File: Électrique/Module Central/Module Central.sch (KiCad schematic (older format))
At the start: 31 parts, among them J101 2.1mm X 5.5mm Barrel Connector, J102 Prog, J103 Conn_Coaxial, U101 LM2937xMP, U102 ATmega328P-AU, U103 RMF95, U104 FXMA108, Y101 16MHz

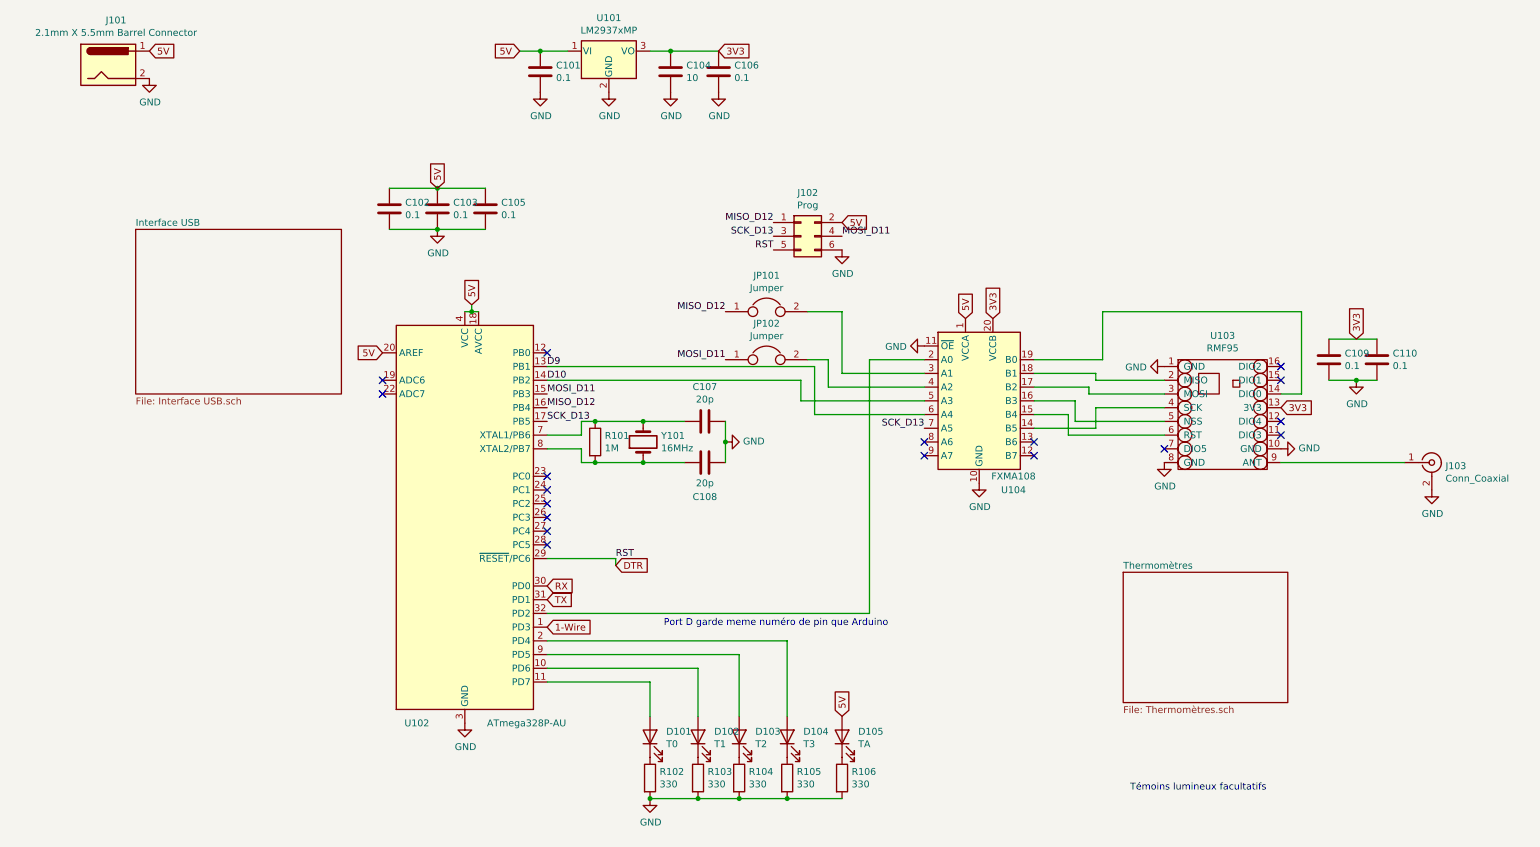
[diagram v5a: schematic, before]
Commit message: Modification PCB
Changement des Level shifters pour des pieces disponibles
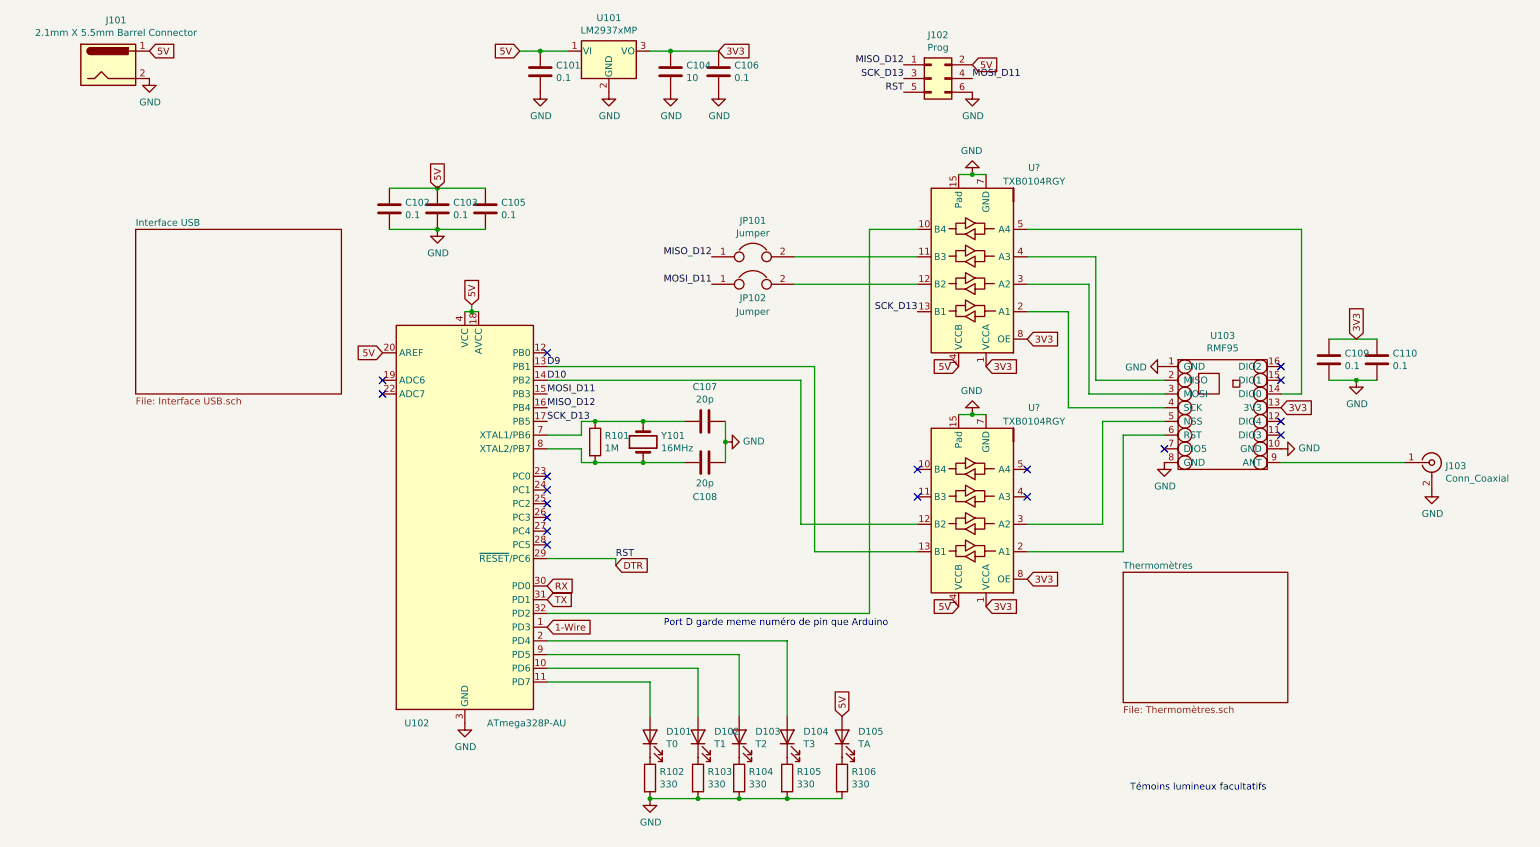
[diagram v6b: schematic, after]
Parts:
- removed U104: FXMA108, Package_DFN_QFN:WQFN-20-1EP_2.5x4.5mm_P0.5mm_EP1x2.9mm, symbol Logic_LevelTranslator:FXMA108
- added U? (x2): TXB0104RGY, Package_DFN_QFN:Texas_S-PVQFN-N14, symbol Logic_LevelTranslator:TXB0104RGY
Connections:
- net 3V3: now also U?.1 (VCCA), U?.1 (VCCA), U?.8 (OE), U?.8 (OE)
- net 5V: now also U?.14 (VCCB), U?.14 (VCCB)
- net D10: now also U?.12 (B2)
- net D9: now also U?.13 (B1)
- net GND: now also U?.15 (Pad), U?.15 (Pad), U?.7 (GND), U?.7 (GND)
- net SCK_D13: now also U?.13 (B1)
- net at U102.32 (PD2): now also U?.10 (B4)
- net at U103.14 (DIO0): now also U?.5 (A4)
- net at U103.2 (MISO): now also U?.4 (A3)
- net at U103.3 (MOSI): now also U?.3 (A2)
- net at U103.4 (SCK): now also U?.2 (A1)
- net at U103.5 (NSS): now also U?.3 (A2)
- net at U103.6 (RST): now also U?.2 (A1)
- net at JP101.2: now also U?.11 (B3)
- net at JP102.2: now also U?.12 (B2)
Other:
- moved on the sheet: J102, JP101, JP102
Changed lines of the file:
@@
 L Connector_Generic:Conn_02x03_Odd_Even J102
 U 1 1 6006D884
-P 6300 2250
-F 0 "J102" H 6350 2567 50  0000 C CNN
-F 1 "Prog" H 6350 2476 50  0000 C CNN
-F 2 "Connector_PinSocket_2.54mm:PinSocket_2x03_P2.54mm_Vertical" H 6300 2250 50  0001 C CNN
-F 3 "~" H 6300 2250 50  0001 C CNN
-	1    6300 2250
+P 7250 1100
+F 0 "J102" H 7300 1417 50  0000 C CNN
+F 1 "Prog" H 7300 1326 50  0000 C CNN
+F 2 "Connector_PinSocket_2.54mm:PinSocket_2x03_P2.54mm_Vertical" H 7250 1100 50  0001 C CNN
+F 3 "~" H 7250 1100 50  0001 C CNN
+	1    7250 1100
 	1    0    0    -1
 $EndComp
@@
 	4450 3300 6300 3300
 Wire Wire Line
-	6300 3300 6300 3450
-Wire Wire Line
 	4450 3200 6400 3200
-Wire Wire Line
-	6400 3200 6400 3550
 Text Label 4450 3200 0    50   ~ 0
 D9
 Text Label 4450 3300 0    50   ~ 0
 D10
-Text Label 6100 2150 2    50   ~ 0
+Text Label 7050 1000 2    50   ~ 0
 MISO_D12
-Text Label 6100 2250 2    50   ~ 0
+Text Label 7050 1100 2    50   ~ 0
 SCK_D13
-Text Label 6100 2350 2    50   ~ 0
+Text Label 7050 1200 2    50   ~ 0
 RST
-Text Label 6600 2250 0    50   ~ 0
+Text Label 7550 1100 0    50   ~ 0
 MOSI_D11
 $Comp
 L power:GND #PWR0110
 U 1 1 6007189E
-P 6600 2350
-F 0 "#PWR0110" H 6600 2100 50  0001 C CNN
-F 1 "GND" H 6605 2177 50  0000 C CNN
-F 2 "" H 6600 2350 50  0001 C CNN
-F 3 "" H 6600 2350 50  0001 C CNN
-	1    6600 2350
-	1    0    0    -1
-$EndComp
-Text GLabel 6600 2150 2    50   Input ~ 0
+P 7550 1200
+F 0 "#PWR0110" H 7550 950 50  0001 C CNN
+F 1 "GND" H 7555 1027 50  0000 C CNN
+F 2 "" H 7550 1200 50  0001 C CNN
+F 3 "" H 7550 1200 50  0001 C CNN
+	1    7550 1200
+	1    0    0    -1
+$EndComp
+Text GLabel 7550 1000 2    50   Input ~ 0
 5V
 Text Label 4950 4600 0    50   ~ 0
@@
 L Device:Jumper JP101
 U 1 1 60072B85
-P 6050 2800
-F 0 "JP101" H 6050 3064 50  0000 C CNN
-F 1 "Jumper" H 6050 2973 50  0000 C CNN
-F 2 "Jumper:SolderJumper-2_P1.3mm_Open_Pad1.0x1.5mm" H 6050 2800 50  0001 C CNN
-F 3 "~" H 6050 2800 50  0001 C CNN
-	1    6050 2800
+P 5950 2400
+F 0 "JP101" H 5950 2664 50  0000 C CNN
+F 1 "Jumper" H 5950 2573 50  0000 C CNN
+F 2 "Jumper:SolderJumper-2_P1.3mm_Open_Pad1.0x1.5mm" H 5950 2400 50  0001 C CNN
+F 3 "~" H 5950 2400 50  0001 C CNN
+	1    5950 2400
 	1    0    0    -1
 $EndComp
@@
 L Device:Jumper JP102
 U 1 1 60074EF6
-P 6050 3150
-F 0 "JP102" H 6050 3414 50  0000 C CNN
-F 1 "Jumper" H 6050 3323 50  0000 C CNN
-F 2 "Jumper:SolderJumper-2_P1.3mm_Open_Pad1.0x1.5mm" H 6050 3150 50  0001 C CNN
-F 3 "~" H 6050 3150 50  0001 C CNN
-	1    6050 3150
-	1    0    0    -1
-$EndComp
-Wire Wire Line
-	6350 3150 6500 3150
-Wire Wire Line
-	6500 3150 6500 3350
-Wire Wire Line
-	6600 3250 6600 2800
-Wire Wire Line
-	6600 2800 6350 2800
-Text Label 5750 2800 2    50   ~ 0
+P 5950 2600
+F 0 "JP102" H 5950 2500 50  0000 C CNN
+F 1 "Jumper" H 5950 2400 50  0000 C CNN
+F 2 "Jumper:SolderJumper-2_P1.3mm_Open_Pad1.0x1.5mm" H 5950 2600 50  0001 C CNN
+F 3 "~" H 5950 2600 50  0001 C CNN
+	1    5950 2600
+	1    0    0    -1
+$EndComp
+Text Label 5650 2400 2    50   ~ 0
 MISO_D12
-Text Label 5750 3150 2    50   ~ 0
+Text Label 5650 2600 2    50   ~ 0
 MOSI_D11
 $Comp
@@
 	5200 6350 5550 6350
 Wire Wire Line
-	8250 3550 8250 3700
-Wire Wire Line
-	8250 3700 8950 3700
-Wire Wire Line
-	8300 3450 8300 3600
-Wire Wire Line
-	8300 3600 8950 3600
-Wire Wire Line
-	8400 3350 8400 3400
-Wire Wire Line
 	8400 3400 8950 3400
 Wire Wire Line
-	8450 3250 8450 3300
-Wire Wire Line
 	8450 3300 8950 3300
 Wire Wire Line
 	9800 3400 9950 3400
 Wire Wire Line
-	9950 3400 9950 2800
-Wire Wire Line
-	9950 2800 8500 2800
-Wire Wire Line
-	8500 2800 8500 3150
-Wire Wire Line
-	7200 3550 6400 3550
-Wire Wire Line
-	7200 3450 6300 3450
-Wire Wire Line
-	6500 3350 7200 3350
-Wire Wire Line
-	6600 3250 7200 3250
-Wire Wire Line
 	4450 5000 6800 5000
-Wire Wire Line
-	6800 5000 6800 3150
-Wire Wire Line
-	6800 3150 7200 3150
-$Comp
-L Logic_LevelTranslator:FXMA108 U104
-U 1 1 60399B14
-P 7600 3450
-F 0 "U104" H 7850 2800 50  0000 C CNN
-F 1 "FXMA108" H 7850 2900 50  0000 C CNN
-F 2 "Package_DFN_QFN:WQFN-20-1EP_2.5x4.5mm_P0.5mm_EP1x2.9mm" H 7600 2750 50  0001 C CNN
-F 3 "http://www.onsemi.com/pub/Collateral/FXMA108-D.pdf" H 7600 3500 50  0001 C CNN
-	1    7600 3450
-	1    0    0    -1
-$EndComp
-NoConn ~ 7200 3750
-NoConn ~ 7200 3850
-Wire Wire Line
-	8500 3150 8000 3150
-Wire Wire Line
-	8450 3250 8000 3250
-Wire Wire Line
-	8400 3350 8000 3350
-Wire Wire Line
-	8300 3450 8000 3450
-Wire Wire Line
-	8250 3550 8000 3550
-NoConn ~ 8000 3750
-NoConn ~ 8000 3850
-$Comp
-L power:GND #PWR0116
-U 1 1 603B0F0C
-P 7200 3050
-F 0 "#PWR0116" H 7200 2800 50  0001 C CNN
-F 1 "GND" V 7205 2922 50  0000 R CNN
-F 2 "" H 7200 3050 50  0001 C CNN
-F 3 "" H 7200 3050 50  0001 C CNN
-	1    7200 3050
-	0    1    1    0
-$EndComp
-Text GLabel 7500 2850 1    50   Input ~ 0
-5V
-Text GLabel 7700 2850 1    50   Input ~ 0
-3V3
-$Comp
-L power:GND #PWR0117
-U 1 1 603B1E4F
-P 7600 4050
-F 0 "#PWR0117" H 7600 3800 50  0001 C CNN
-F 1 "GND" H 7605 3877 50  0000 C CNN
-F 2 "" H 7600 4050 50  0001 C CNN
-F 3 "" H 7600 4050 50  0001 C CNN
-	1    7600 4050
-	1    0    0    -1
-$EndComp
 Connection ~ 5200 6350
 Connection ~ 5550 6350
@@
 Text Label 4450 3600 0    50   ~ 0
 SCK_D13
-Text Label 7200 3650 2    50   ~ 0
+Text Label 7150 2800 2    50   ~ 0
 SCK_D13
-Wire Wire Line
-	8000 3650 8450 3650
-Wire Wire Line
-	8450 3650 8450 3500
-Wire Wire Line
-	8450 3500 8950 3500
+$Comp
+L Logic_LevelTranslator:TXB0104RGY U?
+U 1 1 6050E4CE
+P 7550 2500
+F 0 "U?" H 7100 1750 50  0000 C CNN
+F 1 "TXB0104RGY" H 7100 1850 50  0000 C CNN
+F 2 "Package_DFN_QFN:Texas_S-PVQFN-N14" H 7550 1750 50  0001 C CNN
+F 3 "http://www.ti.com/lit/ds/symlink/txb0104.pdf" H 7660 2595 50  0001 C CNN
+	1    7550 2500
+	-1   0    0    1
+$EndComp
+$Comp
+L power:GND #PWR?
+U 1 1 605187C6
+P 7550 1800
+F 0 "#PWR?" H 7550 1550 50  0001 C CNN
+F 1 "GND" H 7555 1627 50  0000 C CNN
+F 2 "" H 7550 1800 50  0001 C CNN
+F 3 "" H 7550 1800 50  0001 C CNN
+	1    7550 1800
+	-1   0    0    1
+$EndComp
+Wire Wire Line
+	7450 1800 7550 1800
+Connection ~ 7550 1800
+Wire Wire Line
+	7550 1800 7650 1800
+Wire Wire Line
+	9950 2200 7950 2200
+Wire Wire Line
+	9950 2200 9950 3400
+Wire Wire Line
+	6800 2200 7150 2200
+Wire Wire Line
+	6800 2200 6800 5000
+Wire Wire Line
+	6250 2400 7150 2400
+Wire Wire Line
+	8450 2400 7950 2400
+Wire Wire Line
+	8450 2400 8450 3300
+Wire Wire Line
+	8400 2600 7950 2600
+Wire Wire Line
+	8400 2600 8400 3400
+Wire Wire Line
+	6250 2600 7150 2600
+Wire Wire Line
+	8250 3500 8250 2800
+Wire Wire Line
+	8250 2800 7950 2800
+Wire Wire Line
+	8250 3500 8950 3500
+Text GLabel 7650 3200 2    50   Input ~ 0
+3V3
+Text GLabel 7450 3200 0    50   Input ~ 0
+5V
+$Comp
+L Logic_LevelTranslator:TXB0104RGY U?
+U 1 1 60552E2F
+P 7550 4250
+F 0 "U?" H 7100 3500 50  0000 C CNN
+F 1 "TXB0104RGY" H 7100 3600 50  0000 C CNN
+F 2 "Package_DFN_QFN:Texas_S-PVQFN-N14" H 7550 3500 50  0001 C CNN
+F 3 "http://www.ti.com/lit/ds/symlink/txb0104.pdf" H 7660 4345 50  0001 C CNN
+	1    7550 4250
+	-1   0    0    1
+$EndComp
+$Comp
+L power:GND #PWR?
+U 1 1 60552E35
+P 7550 3550
+F 0 "#PWR?" H 7550 3300 50  0001 C CNN
+F 1 "GND" H 7555 3377 50  0000 C CNN
+F 2 "" H 7550 3550 50  0001 C CNN
+F 3 "" H 7550 3550 50  0001 C CNN
+	1    7550 3550
+	-1   0    0    1
+$EndComp
+Wire Wire Line
+	7450 3550 7550 3550
+Connection ~ 7550 3550
+Wire Wire Line
+	7550 3550 7650 3550
+Text GLabel 7650 4950 2    50   Input ~ 0
+3V3
+Text GLabel 7450 4950 0    50   Input ~ 0
+5V
+Wire Wire Line
+	8950 3700 8650 3700
+Wire Wire Line
+	8650 3700 8650 4550
+Wire Wire Line
+	8650 4550 7950 4550
+Wire Wire Line
+	8950 3600 8500 3600
+Wire Wire Line
+	8500 3600 8500 4350
+Wire Wire Line
+	8500 4350 7950 4350
+Wire Wire Line
+	6400 4550 7150 4550
+Wire Wire Line
+	6400 3200 6400 4550
+Wire Wire Line
+	6300 4350 7150 4350
+Wire Wire Line
+	6300 3300 6300 4350
+Text GLabel 7950 3000 2    50   Input ~ 0
+3V3
+Text GLabel 7950 4750 2    50   Input ~ 0
+3V3
+NoConn ~ 7150 3950
+NoConn ~ 7150 4150
+NoConn ~ 7950 3950
+NoConn ~ 7950 4150
 $EndSCHEMATC

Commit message: Modif PCB en cours
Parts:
- added JP103, JP104: Jumper, Connector_PinSocket_2.54mm:PinSocket_1x02_P2.54mm_Vertical, symbol Device:Jumper
- added R107, R108: 1K, Resistor_SMD:R_0805_2012Metric, symbol Device:R
- gave numbers to parts that had none: 2
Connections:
- net 3V3: now also JP103.2, JP104.2; no longer U104.8 (OE), U105.8 (OE)
- net GND: now also R107.2, R108.2
- new net: JP104.1, R107.1, U104.8 (OE)
- new net: JP103.1, R108.1, U105.8 (OE)
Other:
- moved on the sheet: C109, C110, U103

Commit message: PCB Avec 2x 4Channel LevelShifters
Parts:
- removed JP103, JP104: Jumper, Connector_PinSocket_2.54mm:PinSocket_1x02_P2.54mm_Vertical, symbol Device:Jumper
- removed R107, R108: 1K, Resistor_SMD:R_0805_2012Metric, symbol Device:R
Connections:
- net 3V3: now also U104.8 (OE), U105.8 (OE)
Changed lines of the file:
@@
 Wire Wire Line
 	6300 3300 6300 4350
-Text GLabel 8350 3600 2    50   Input ~ 0
+Text GLabel 8350 3000 2    50   Input ~ 0
 3V3
 NoConn ~ 7150 3950
@@
 Wire Wire Line
 	8850 3400 9450 3400
-$Comp
-L Device:R R108
-U 1 1 60571DFE
-P 8050 4900
-F 0 "R108" H 8120 4946 50  0000 L CNN
-F 1 "1K" H 8120 4855 50  0000 L CNN
-F 2 "Resistor_SMD:R_0805_2012Metric" V 7980 4900 50  0001 C CNN
-F 3 "~" H 8050 4900 50  0001 C CNN
-	1    8050 4900
-	1    0    0    -1
-$EndComp
-Connection ~ 8050 4750
-Wire Wire Line
-	8050 4750 7950 4750
-$Comp
-L power:GND #PWR0119
-U 1 1 605744CB
-P 8050 5050
-F 0 "#PWR0119" H 8050 4800 50  0001 C CNN
-F 1 "GND" H 8055 4877 50  0000 C CNN
-F 2 "" H 8050 5050 50  0001 C CNN
-F 3 "" H 8050 5050 50  0001 C CNN
-	1    8050 5050
-	1    0    0    -1
-$EndComp
-$Comp
-L Device:R R107
-U 1 1 605746AE
-P 8050 3150
-F 0 "R107" H 8120 3196 50  0000 L CNN
-F 1 "1K" H 8120 3105 50  0000 L CNN
-F 2 "Resistor_SMD:R_0805_2012Metric" V 7980 3150 50  0001 C CNN
-F 3 "~" H 8050 3150 50  0001 C CNN
-	1    8050 3150
-	1    0    0    -1
-$EndComp
-Connection ~ 8050 3000
-Wire Wire Line
-	8050 3000 7950 3000
-$Comp
-L power:GND #PWR0118
-U 1 1 605770D2
-P 8050 3300
-F 0 "#PWR0118" H 8050 3050 50  0001 C CNN
-F 1 "GND" H 8055 3127 50  0000 C CNN
-F 2 "" H 8050 3300 50  0001 C CNN
-F 3 "" H 8050 3300 50  0001 C CNN
-	1    8050 3300
-	1    0    0    -1
-$EndComp
 Wire Wire Line
 	10700 3900 10300 3900
@@
 Wire Wire Line
 	7950 4550 9150 4550
-$Comp
-L Device:Jumper JP104
-U 1 1 6058F414
-P 8350 3300
-F 0 "JP104" V 8304 3427 50  0000 L CNN
-F 1 "Jumper" V 8395 3427 50  0000 L CNN
-F 2 "Connector_PinSocket_2.54mm:PinSocket_1x02_P2.54mm_Vertical" H 8350 3300 50  0001 C CNN
-F 3 "~" H 8350 3300 50  0001 C CNN
-	1    8350 3300
-	0    1    1    0
-$EndComp
+Text GLabel 8300 4750 2    50   Input ~ 0
+3V3
 Wire Wire Line
-	8050 3000 8350 3000
-Text GLabel 8300 5350 2    50   Input ~ 0
-3V3
-$Comp
-L Device:Jumper JP103
-U 1 1 6059448D
-P 8300 5050
-F 0 "JP103" V 8254 5177 50  0000 L CNN
-F 1 "Jumper" V 8345 5177 50  0000 L CNN
-F 2 "Connector_PinSocket_2.54mm:PinSocket_1x02_P2.54mm_Vertical" H 8300 5050 50  0001 C CNN
-F 3 "~" H 8300 5050 50  0001 C CNN
-	1    8300 5050
-	0    1    1    0
-$EndComp
+	7950 4750 8300 4750
 Wire Wire Line
-	8050 4750 8300 4750
+	7950 3000 8350 3000
 $EndSCHEMATC
